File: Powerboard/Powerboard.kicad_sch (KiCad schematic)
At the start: 8 parts, among them IC1 TEENSY_4.1, J1 Screw_Terminal_01x02, J2 1993776, J3 Screw_Terminal_01x12, J4 Screw_Terminal_01x06, J5 Screw_Terminal_01x06, J6 Screw_Terminal_01x06, J7 Screw_Terminal_01x12

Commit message: Updated
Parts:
- removed J4, J6: Screw_Terminal_01x06, TerminalBlock_Phoenix:TerminalBlock_Phoenix_MKDS-1,5-6_1x06_P5.00mm_Horizontal, symbol Connector:Screw_Terminal_01x06
- added J3: 1993776, 1993776:PHOENIX_1993776, symbol 1993776:1993776
- J1: renamed from J5; footprint TerminalBlock_Phoenix:TerminalBlock_Phoenix_MKDS-1,5-6_1x06_P5.00mm_Horizontal -> TerminalBlock_Phoenix:TerminalBlock_Phoenix_MPT-0,5-6-2.54_1x06_P2.54mm_Horizontal
- J4: renamed from J3; footprint TerminalBlock_Phoenix:TerminalBlock_Phoenix_MKDS-1,5-12-5.08_1x12_P5.08mm_Horizontal -> TerminalBlock_Phoenix:TerminalBlock_Phoenix_MPT-0,5-12-2.54_1x12_P2.54mm_Horizontal
- J5: renamed from J7; footprint TerminalBlock_Phoenix:TerminalBlock_Phoenix_MKDS-1,5-12-5.08_1x12_P5.08mm_Horizontal -> TerminalBlock_Phoenix:TerminalBlock_Phoenix_MPT-0,5-12-2.54_1x12_P2.54mm_Horizontal
- renumbered J1 to J2, J2 to J6
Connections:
- net GND: now also J6.1_1, J6.1_2
- net Vout_3v3: now also J3.1_1, J3.1_2
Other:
- moved on the sheet: J6

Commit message: update
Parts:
- added H1, H2, H3, H4: MountingHole, MountingHole:MountingHole_3.2mm_M3_Pad_Via, symbol Mechanical:MountingHole

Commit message: Pre-DRC Done
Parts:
- H1, H2, H3, H4: footprint MountingHole:MountingHole_3.2mm_M3_Pad_Via -> MountingHole:MountingHole_3.2mm_M3_Pad
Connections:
- net EA1_3v3: now also IC1.16 (A2); no longer IC1.23 (A9)
- net EA2_3v3: now also IC1.18 (A4); no longer IC1.21 (A7)
- net EA3_3v3: now also IC1.20 (A6); no longer IC1.19 (A5)
- net EA4_3v3: now also IC1.22 (A8); no longer IC1.17 (A3)
- net EB1_3v3: now also IC1.17 (A3); no longer IC1.22 (A8)
- net EB2_3v3: now also IC1.19 (A5); no longer IC1.20 (A6)
- net EB3_3v3: now also IC1.21 (A7); no longer IC1.18 (A4)
- net EB4_3v3: now also IC1.23 (A9); no longer IC1.16 (A2)
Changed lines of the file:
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@@
 	)
 	(label "EA4_3v3"
-		(at 135.89 64.77 180)
+		(at 135.89 77.47 180)
 		(effects
 			(font
@@
 	)
 	(label "EB4_3v3"
-		(at 135.89 62.23 180)
+		(at 135.89 80.01 180)
 		(effects
 			(font
@@
 	)
 	(label "EB3_3v3"
-		(at 135.89 67.31 180)
+		(at 135.89 74.93 180)
 		(effects
 			(font
@@
 	)
 	(label "EB1_3v3"
-		(at 135.89 77.47 180)
+		(at 135.89 64.77 180)
 		(effects
 			(font
@@
 	)
 	(label "EA1_3v3"
-		(at 135.89 80.01 180)
+		(at 135.89 62.23 180)
 		(effects
 			(font
@@
 	)
 	(label "EA2_3v3"
-		(at 135.89 74.93 180)
+		(at 135.89 67.31 180)
 		(effects
 			(font
@@
 	)
 	(label "EB2_3v3"
-		(at 135.89 72.39 180)
+		(at 135.89 69.85 180)
 		(effects
 			(font
@@
 	)
 	(label "EA3_3v3"
-		(at 135.89 69.85 180)
+		(at 135.89 72.39 180)
 		(effects
 			(font
@@
 			)
 		)
-		(property "Footprint" "MountingHole:MountingHole_3.2mm_M3_Pad_Via"
+		(property "Footprint" "MountingHole:MountingHole_3.2mm_M3_Pad"
 			(at 152.4 121.92 0)
 			(hide yes)
@@
 			)
 		)
-		(property "Footprint" "MountingHole:MountingHole_3.2mm_M3_Pad_Via"
+		(property "Footprint" "MountingHole:MountingHole_3.2mm_M3_Pad"
 			(at 152.4 127 0)
 			(hide yes)
@@
 			)
 		)
-		(property "Footprint" "MountingHole:MountingHole_3.2mm_M3_Pad_Via"
+		(property "Footprint" "MountingHole:MountingHole_3.2mm_M3_Pad"
 			(at 152.4 116.84 0)
 			(hide yes)
@@
 			)
 		)
-		(property "Footprint" "MountingHole:MountingHole_3.2mm_M3_Pad_Via"
+		(property "Footprint" "MountingHole:MountingHole_3.2mm_M3_Pad"
 			(at 152.4 132.08 0)
 			(hide yes)

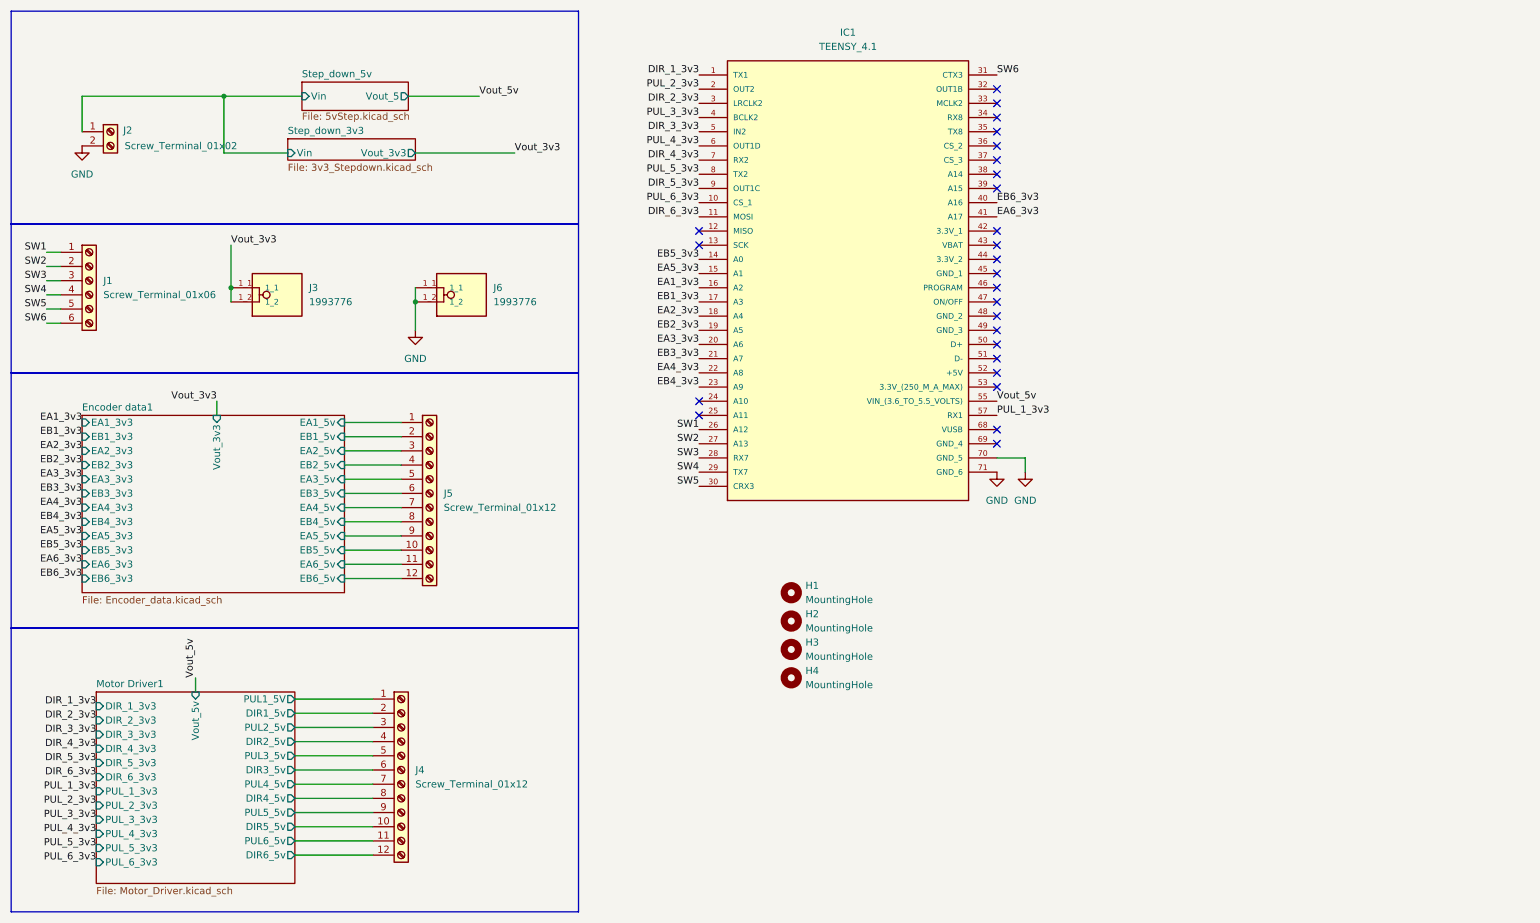
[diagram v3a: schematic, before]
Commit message: Rev1.1 Done
Finished the board ran DRC all clear
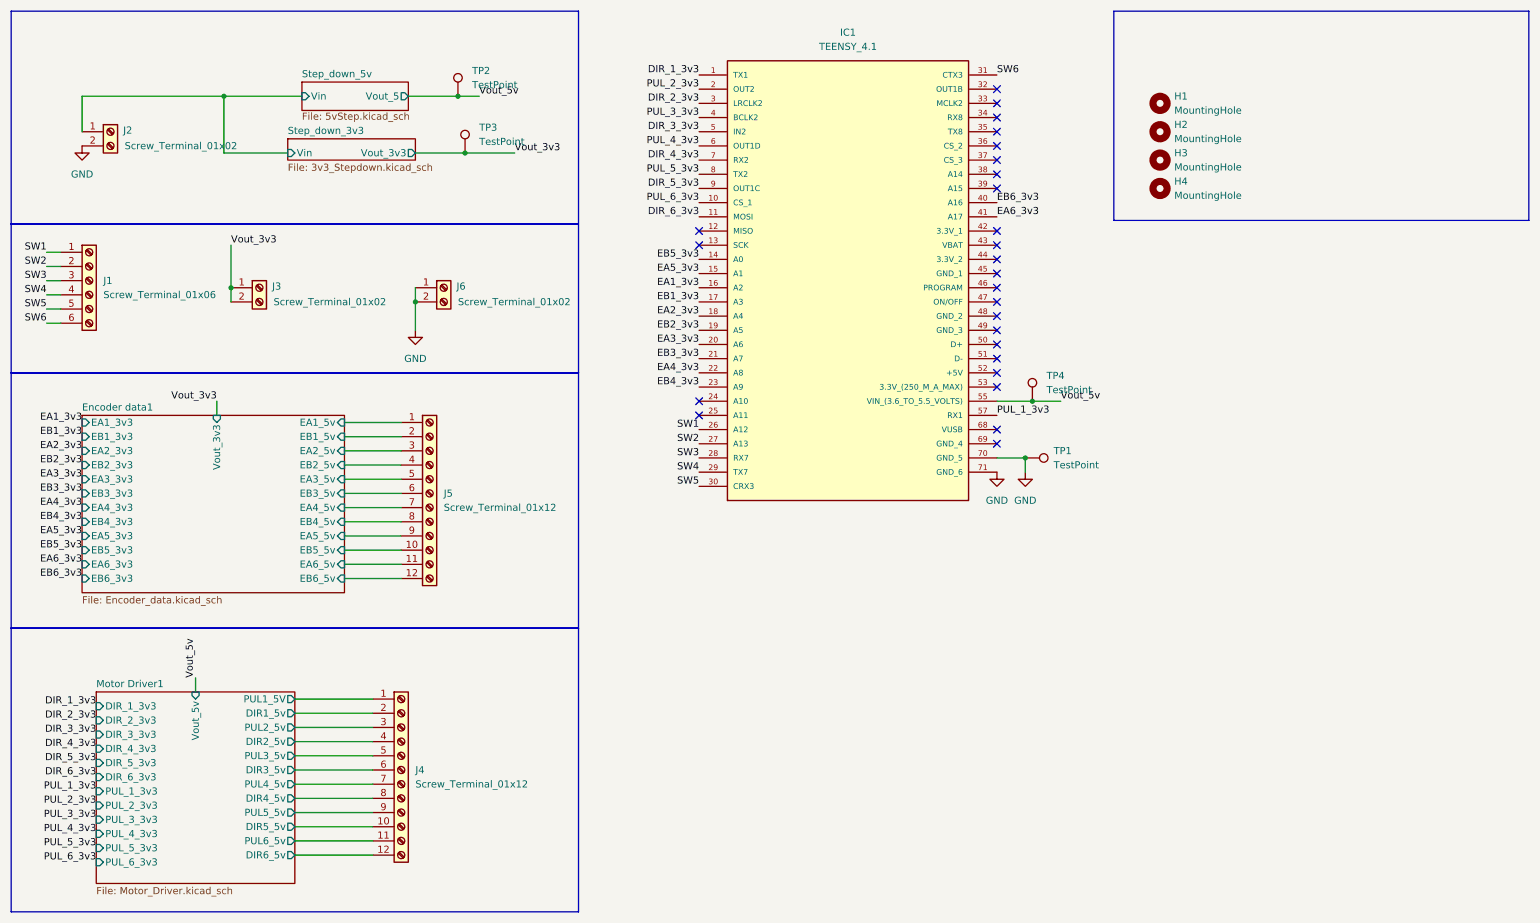
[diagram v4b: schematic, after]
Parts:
- removed J3, J6: 1993776, 1993776:PHOENIX_1993776, symbol 1993776:1993776
- added J3, J6: Screw_Terminal_01x02, TerminalBlock_Phoenix:TerminalBlock_Phoenix_PT-1,5-2-5.0-H_1x02_P5.00mm_Horizontal, symbol Connector:Screw_Terminal_01x02
- added TP1, TP2, TP3, TP4: TestPoint, TestPoint:TestPoint_Pad_D1.5mm, symbol Connector:TestPoint
- H1, H2, H3, H4: footprint MountingHole:MountingHole_3.2mm_M3_Pad -> MountingHole:MountingHole_3.2mm_M3_Pad_Via
- J2: footprint TerminalBlock_Altech:Altech_AK100_1x02_P5.00mm -> TerminalBlock_Phoenix:TerminalBlock_Phoenix_PT-1,5-2-5.0-H_1x02_P5.00mm_Horizontal
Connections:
- net GND: now also J6.1 (Pin_1), J6.2 (Pin_2), TP1.1
- net Vout_3v3: now also J3.1 (Pin_1), J3.2 (Pin_2), TP3.1
- net Vout_5v: now also TP2.1, TP4.1
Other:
- company: (none) -> Visionbyte Labs
- title: (none) -> Arm Powerboard
- moved on the sheet: H1, H2, H3, H4

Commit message: Replaced HCT->ACT
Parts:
- added J7: Screw_Terminal_01x02, TerminalBlock_Phoenix:TerminalBlock_Phoenix_MPT-0,5-2-2.54_1x02_P2.54mm_Horizontal, symbol Connector:Screw_Terminal_01x02
- renumbered TP2 to TP1, TP3 to TP2, TP1 to TP3
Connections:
- net GND: now also J7.1 (Pin_1)
- net at IC1.24 (A10): now also J7.2 (Pin_2)
- no-connect marks 26 -> 25
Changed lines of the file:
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@@
-	)
-	(no_connect
-		(at 135.89 82.55)
 	)
 	(no_connect
@@
 	(wire
 		(pts
+			(xy 124.46 90.17) (xy 124.46 97.79)
+		)
+		(stroke
+			(width 0)
+			(type default)
+		)
+	)
+	(wire
+		(pts
 			(xy 82.55 93.98) (xy 72.39 93.98)
 		)
@@
 	(wire
 		(pts
+			(xy 124.46 82.55) (xy 135.89 82.55)
+		)
+		(stroke
+			(width 0)
+			(type default)
+		)
+	)
+	(wire
+		(pts
 			(xy 194.31 92.71) (xy 194.31 95.25)
 		)
@@
 		(pts
 			(xy 85.09 64.77) (xy 85.09 69.85)
+		)
+		(stroke
+			(width 0)
+			(type default)
+		)
+	)
+	(wire
+		(pts
+			(xy 124.46 82.55) (xy 124.46 87.63)
 		)
 		(stroke
@@
 		(dnp no)
 		(fields_autoplaced yes)
-		(property "Reference" "TP1"
+		(property "Reference" "TP3"
 			(at 199.39 91.4399 90)
 			(show_name no)
@@
 			(project "Powerboard"
 				(path "/07aca59a-bf87-409f-a974-db5a163ccf8c"
-					(reference "TP1")
+					(reference "TP3")
+					(unit 1)
+				)
+			)
+		)
+	)
+	(symbol
+		(lib_id "Connector:Screw_Terminal_01x02")
+		(at 119.38 90.17 180)
+		(unit 1)
+		(body_style 1)
+		(exclude_from_sim no)
+		(in_bom yes)
+		(on_board yes)
+		(in_pos_files yes)
+		(dnp no)
+		(property "Reference" "J7"
+			(at 117.094 90.424 0)
+			(show_name no)
+			(do_not_autoplace no)
+			(effects
+				(font
+					(size 1.27 1.27)
+				)
+				(justify left)
+			)
+		)
+		(property "Value" "Screw_Terminal_01x02"
+			(at 116.84 87.6301 0)
+			(show_name no)
+			(do_not_autoplace no)
+			(effects
+				(font
+					(size 1.27 1.27)
+				)
+				(justify left)
+			)
+		)
+		(property "Footprint" "TerminalBlock_Phoenix:TerminalBlock_Phoenix_MPT-0,5-2-2.54_1x02_P2.54mm_Horizontal"
+			(at 119.38 90.17 0)
+			(hide yes)
+			(show_name no)
+			(do_not_autoplace no)
+			(effects
+				(font
+					(size 1.27 1.27)
+				)
+			)
+		)
+		(property "Datasheet" ""
+			(at 119.38 90.17 0)
+			(hide yes)
+			(show_name no)
+			(do_not_autoplace no)
+			(effects
+				(font
+					(size 1.27 1.27)
+				)
+			)
+		)
+		(property "Description" "Generic screw terminal, single row, 01x02, script generated (kicad-library-utils/schlib/autogen/connector/)"
+			(at 119.38 90.17 0)
+			(hide yes)
+			(show_name no)
+			(do_not_autoplace no)
+			(effects
+				(font
+					(size 1.27 1.27)
+				)
+			)
+		)
+		(property "Untitled Field" ""
+			(at 119.38 90.17 0)
+			(hide yes)
+			(show_name no)
+			(do_not_autoplace no)
+			(effects
+				(font
+					(size 1.27 1.27)
+				)
+			)
+		)
+		(pin "1"
+		)
+		(pin "2"
+		)
+		(instances
+			(project "Powerboard"
+				(path "/07aca59a-bf87-409f-a974-db5a163ccf8c"
+					(reference "J7")
 					(unit 1)
 				)
@@
 		(dnp no)
 		(fields_autoplaced yes)
-		(property "Reference" "TP3"
+		(property "Reference" "TP2"
 			(at 96.52 33.5279 0)
 			(show_name no)
@@
 			(project "Powerboard"
 				(path "/07aca59a-bf87-409f-a974-db5a163ccf8c"
-					(reference "TP3")
+					(reference "TP2")
 					(unit 1)
 				)
@@
 	)
 	(symbol
+		(lib_id "power:GND")
+		(at 124.46 97.79 0)
+		(unit 1)
+		(body_style 1)
+		(exclude_from_sim no)
+		(in_bom yes)
+		(on_board yes)
+		(in_pos_files yes)
+		(dnp no)
+		(fields_autoplaced yes)
+		(property "Reference" "#PWR03"
+			(at 124.46 104.14 0)
+			(hide yes)
+			(show_name no)
+			(do_not_autoplace no)
+			(effects
+				(font
+					(size 1.27 1.27)
+				)
+			)
+		)
+		(property "Value" "GND"
+			(at 124.46 102.87 0)
+			(show_name no)
+			(do_not_autoplace no)
+			(effects
+				(font
+					(size 1.27 1.27)
+				)
+			)
+		)
+		(property "Footprint" ""
+			(at 124.46 97.79 0)
+			(hide yes)
+			(show_name no)
+			(do_not_autoplace no)
+			(effects
+				(font
+					(size 1.27 1.27)
+				)
+			)
+		)
+		(property "Datasheet" ""
+			(at 124.46 97.79 0)
+			(hide yes)
+			(show_name no)
+			(do_not_autoplace no)
+			(effects
+				(font
+					(size 1.27 1.27)
+				)
+			)
+		)
+		(property "Description" "Power symbol creates a global label with name \"GND\" , ground"
+			(at 124.46 97.79 0)
+			(hide yes)
+			(show_name no)
+			(do_not_autoplace no)
+			(effects
+				(font
+					(size 1.27 1.27)
+				)
+			)
+		)
+		(pin "1"
+		)
+		(instances
+			(project "Powerboard"
+				(path "/07aca59a-bf87-409f-a974-db5a163ccf8c"
+					(reference "#PWR03")
+					(unit 1)
+				)
+			)
+		)
+	)
+	(symbol
 		(lib_id "TEENSY_4.1:TEENSY_4.1")
 		(at 135.89 24.13 0)
@@
 		(dnp no)
 		(fields_autoplaced yes)
-		(property "Reference" "#PWR03"
+		(property "Reference" "#PWR04"
 			(at 189.23 101.6 0)
 			(hide yes)
@@
 			(project "Powerboard"
 				(path "/07aca59a-bf87-409f-a974-db5a163ccf8c"
-					(reference "#PWR03")
+					(reference "#PWR04")
 					(unit 1)
 				)
@@
 		(dnp no)
 		(fields_autoplaced yes)
-		(property "Reference" "#PWR04"
+		(property "Reference" "#PWR05"
 			(at 194.31 101.6 0)
 			(hide yes)
@@
 			(project "Powerboard"
 				(path "/07aca59a-bf87-409f-a974-db5a163ccf8c"
-					(reference "#PWR04")
+					(reference "#PWR05")
 					(unit 1)
 				)
@@
 		(dnp no)
 		(fields_autoplaced yes)
-		(property "Reference" "TP2"
+		(property "Reference" "TP1"
 			(at 95.25 23.3679 0)
 			(show_name no)
@@
 			(project "Powerboard"
 				(path "/07aca59a-bf87-409f-a974-db5a163ccf8c"
-					(reference "TP2")
+					(reference "TP1")
 					(unit 1)
 				)
